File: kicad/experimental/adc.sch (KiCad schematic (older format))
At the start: 23 parts, among them J4 PWR_IN, J5 SIG_IN, J6 SPI, U3 L78L05, U4 AD7682BCP

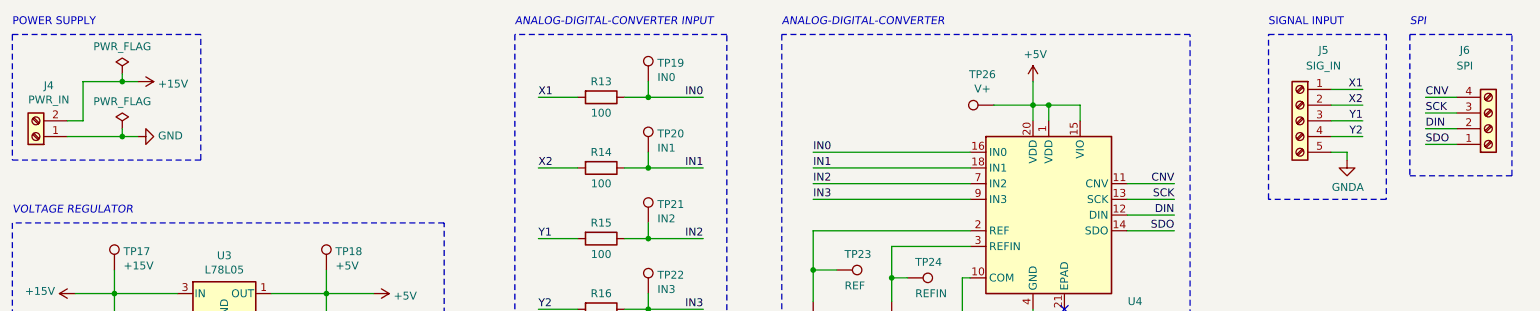
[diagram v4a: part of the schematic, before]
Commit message: completed pcb design of experimental buffer and adc
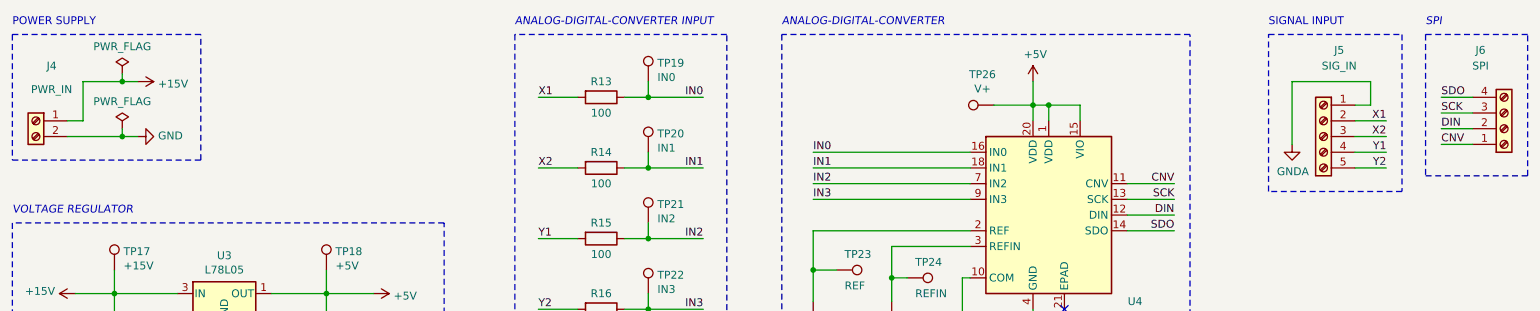
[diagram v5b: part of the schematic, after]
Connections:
- net +15V: now also J4.1 (Pin_1); no longer J4.2 (Pin_2)
- net CNV: now also J6.1 (Pin_1); no longer J6.4 (Pin_4)
- net GND: now also J4.2 (Pin_2); no longer J4.1 (Pin_1)
- net GNDA: now also J5.1 (Pin_1); no longer J5.5 (Pin_5)
- net SDO: now also J6.4 (Pin_4); no longer J6.1 (Pin_1)
- net X1: now also J5.2 (Pin_2); no longer J5.1 (Pin_1)
- net X2: now also J5.3 (Pin_3); no longer J5.2 (Pin_2)
- net Y1: now also J5.4 (Pin_4); no longer J5.3 (Pin_3)
- net Y2: now also J5.5 (Pin_5); no longer J5.4 (Pin_4)
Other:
- moved on the sheet: J5, J6
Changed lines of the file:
@@
 Text Notes 1000 950  0    50   ~ 0
 POWER SUPPLY
-Text Label 9600 1350 2    50   ~ 0
+Text Label 9750 1550 2    50   ~ 0
 X1
 Wire Wire Line
-	9600 1350 9400 1350
-Text Label 9600 1450 2    50   ~ 0
+	9750 1550 9550 1550
+Text Label 9750 1650 2    50   ~ 0
 X2
 Wire Wire Line
-	9600 1450 9400 1450
-Text Label 9600 1550 2    50   ~ 0
+	9750 1650 9550 1650
+Text Label 9750 1750 2    50   ~ 0
 Y1
 Wire Wire Line
-	9600 1550 9400 1550
-Text Label 9600 1650 2    50   ~ 0
+	9750 1750 9550 1750
+Text Label 9750 1850 2    50   ~ 0
 Y2
 Wire Wire Line
-	9600 1650 9400 1650
-Wire Notes Line
-	9000 1000 9750 1000
-Wire Notes Line
-	9750 1000 9750 2050
-Wire Notes Line
-	9750 2050 9000 2050
-Wire Notes Line
-	9000 2050 9000 1000
+	9750 1850 9550 1850
+Wire Notes Line
+	9000 1000 9850 1000
+Wire Notes Line
+	9850 1000 9850 2000
+Wire Notes Line
+	9850 2000 9000 2000
+Wire Notes Line
+	9000 2000 9000 1000
 Text Notes 9000 950  0    50   ~ 0
 SIGNAL INPUT
@@
 L Connector:Screw_Terminal_01x04 J?
 U 1 1 5D6D0047
-P 10400 1600
+P 10500 1600
 AR Path="/5D61C196/5D6D0047" Ref="J?"  Part="1"
 AR Path="/5D601578/5D6D0047" Ref="J6"  Part="1"
-F 0 "J6" H 10250 1100 50  0000 C CNN
-F 1 "SPI" H 10250 1200 50  0000 C CNN
-F 2 "TerminalBlock_TE-Connectivity:TerminalBlock_TE_282834-4_1x04_P2.54mm_Horizontal" H 10400 1600 50  0001 C CNN
-F 3 "~" H 10400 1600 50  0001 C CNN
-	1    10400 1600
+F 0 "J6" H 10350 1100 50  0000 C CNN
+F 1 "SPI" H 10350 1200 50  0000 C CNN
+F 2 "TerminalBlock_TE-Connectivity:TerminalBlock_TE_282834-4_1x04_P2.54mm_Horizontal" H 10500 1600 50  0001 C CNN
+F 3 "~" H 10500 1600 50  0001 C CNN
+	1    10500 1600
 	1    0    0    1
 $EndComp
-Text Label 10000 1400 0    50   ~ 0
+Text Label 10100 1700 0    50   ~ 0
 CNV
 Wire Wire Line
-	10000 1400 10200 1400
-Text Label 10000 1500 0    50   ~ 0
+	10100 1400 10300 1400
+Text Label 10100 1500 0    50   ~ 0
 SCK
 Wire Wire Line
-	10000 1500 10200 1500
-Text Label 10000 1600 0    50   ~ 0
+	10100 1500 10300 1500
+Text Label 10100 1600 0    50   ~ 0
 DIN
 Wire Wire Line
-	10000 1600 10200 1600
-Text Label 10000 1700 0    50   ~ 0
+	10100 1600 10300 1600
+Text Label 10100 1400 0    50   ~ 0
 SDO
 Wire Wire Line
-	10000 1700 10200 1700
-Wire Notes Line
-	10550 1000 9900 1000
-Wire Notes Line
-	9900 1000 9900 1900
-Wire Notes Line
-	9900 1900 10550 1900
-Wire Notes Line
-	10550 1900 10550 1000
-Text Notes 9900 950  0    50   Italic 0
+	10100 1700 10300 1700
+Wire Notes Line
+	10650 1000 10000 1000
+Wire Notes Line
+	10000 1000 10000 1900
+Wire Notes Line
+	10000 1900 10650 1900
+Wire Notes Line
+	10650 1900 10650 1000
+Text Notes 10000 950  0    50   Italic 0
 SPI
 Text Label 4350 1400 0    50   ~ 0
@@
 L Connector:Screw_Terminal_01x05 J5
 U 1 1 5D6F1D26
-P 9200 1550
-F 0 "J5" H 9050 2000 50  0000 C CNN
-F 1 "SIG_IN" H 9050 1900 50  0000 C CNN
-F 2 "TerminalBlock_TE-Connectivity:TerminalBlock_TE_282834-5_1x05_P2.54mm_Horizontal" H 9200 1550 50  0001 C CNN
-F 3 "~" H 9200 1550 50  0001 C CNN
-	1    9200 1550
+P 9350 1650
+F 0 "J5" H 9250 2200 50  0000 C CNN
+F 1 "SIG_IN" H 9250 2100 50  0000 C CNN
+F 2 "TerminalBlock_TE-Connectivity:TerminalBlock_TE_282834-5_1x05_P2.54mm_Horizontal" H 9350 1650 50  0001 C CNN
+F 3 "~" H 9350 1650 50  0001 C CNN
+	1    9350 1650
 	-1   0    0    -1
 $EndComp
-Wire Wire Line
-	9500 1750 9400 1750
 $Comp
 L power:GNDA #PWR028
 U 1 1 5D6F572D
-P 9500 1800
-F 0 "#PWR028" H 9500 1550 50  0001 C CNN
-F 1 "GNDA" H 9505 1627 50  0000 C CNN
-F 2 "" H 9500 1800 50  0001 C CNN
-F 3 "" H 9500 1800 50  0001 C CNN
-	1    9500 1800
-	1    0    0    -1
-$EndComp
-Wire Wire Line
-	9500 1750 9500 1800
+P 9150 1700
+F 0 "#PWR028" H 9150 1450 50  0001 C CNN
+F 1 "GNDA" H 9155 1527 50  0000 C CNN
+F 2 "" H 9150 1700 50  0001 C CNN
+F 3 "" H 9150 1700 50  0001 C CNN
+	1    9150 1700
+	1    0    0    -1
+$EndComp
 $Comp
 L power:GNDA #PWR025
@@
 L Connector:Screw_Terminal_01x02 J4
 U 1 1 5D6FEBEF
-P 1150 1650
-F 0 "J4" H 1068 1325 50  0000 C CNN
-F 1 "PWR_IN" H 1068 1416 50  0000 C CNN
-F 2 "TerminalBlock_TE-Connectivity:TerminalBlock_TE_282834-2_1x02_P2.54mm_Horizontal" H 1150 1650 50  0001 C CNN
-F 3 "~" H 1150 1650 50  0001 C CNN
-	1    1150 1650
-	-1   0    0    1
+P 1150 1550
+F 0 "J4" H 1050 1900 50  0000 C CNN
+F 1 "PWR_IN" H 1050 1750 50  0000 C CNN
+F 2 "TerminalBlock_TE-Connectivity:TerminalBlock_TE_282834-2_1x02_P2.54mm_Horizontal" H 1150 1550 50  0001 C CNN
+F 3 "~" H 1150 1550 50  0001 C CNN
+	1    1150 1550
+	-1   0    0    -1
 $EndComp
 $Comp
@@
 Wire Wire Line
 	6100 2500 6100 2700
+Wire Wire Line
+	9550 1450 9650 1450
+Wire Wire Line
+	9650 1450 9650 1300
+Wire Wire Line
+	9650 1300 9150 1300
+Wire Wire Line
+	9150 1300 9150 1700
 $EndSCHEMATC
